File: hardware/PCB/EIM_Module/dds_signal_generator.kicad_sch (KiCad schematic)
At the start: 48 parts, among them J1 Conn_02x04, U1 AD9834BRUZ, U2 AD8130ARZ, Y2 75MHz

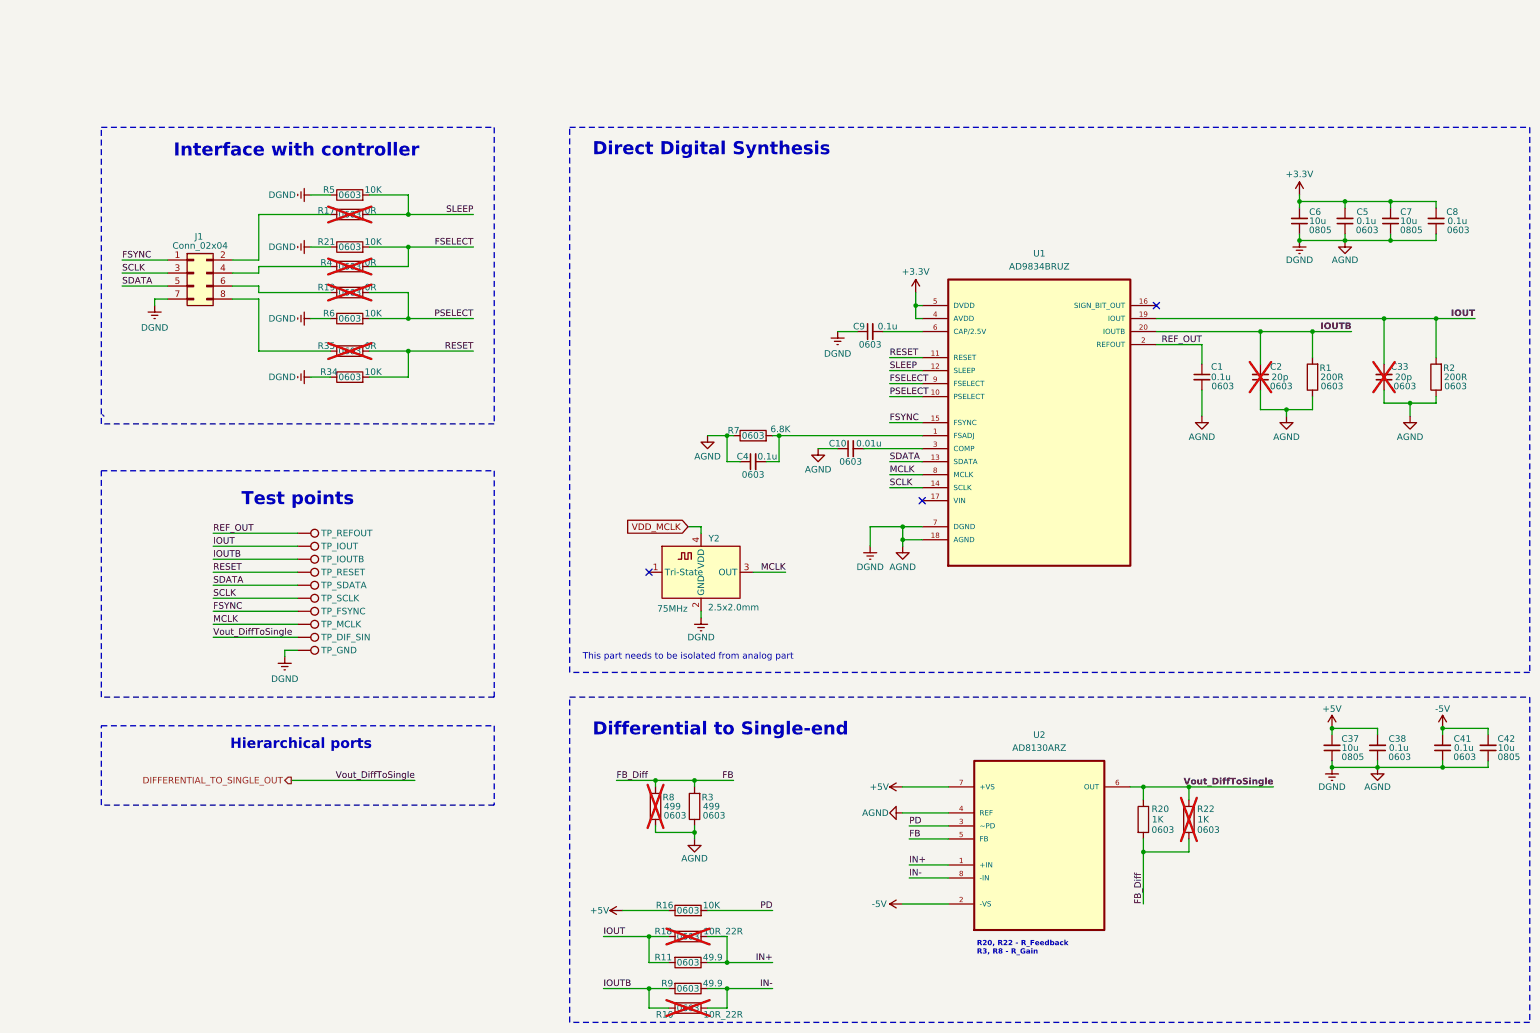
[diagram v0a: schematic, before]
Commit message: MAMS-33 Updated simulation final and update schematic and PCB
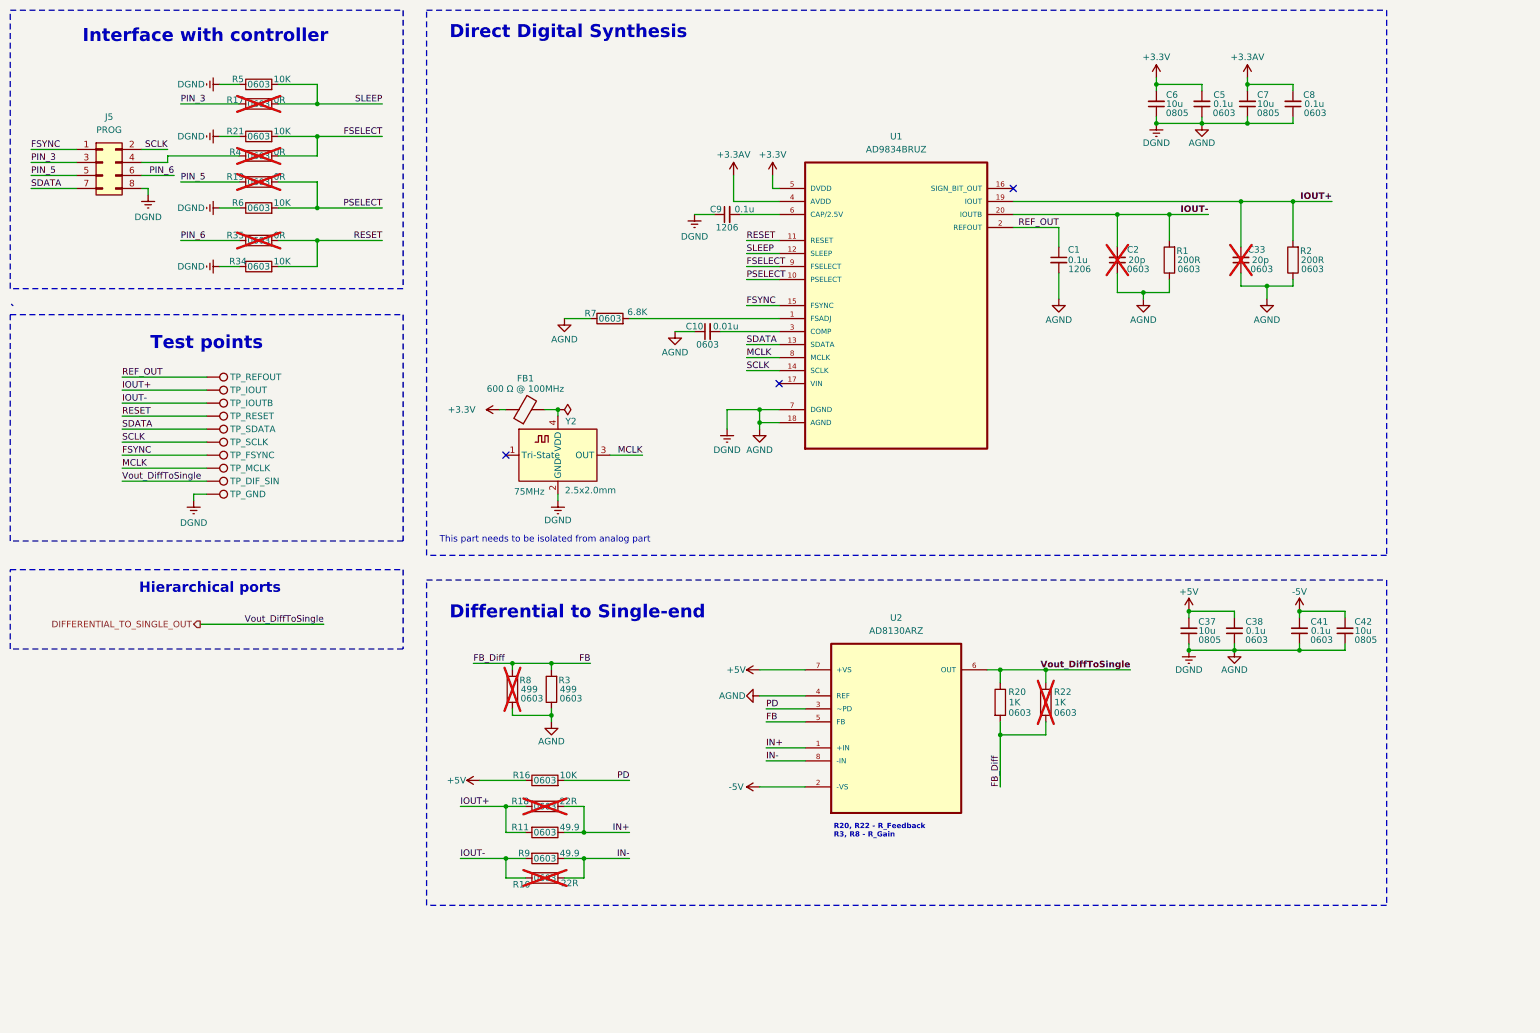
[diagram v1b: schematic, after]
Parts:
- removed C4: 0.1u, Capacitor_SMD:C_0603_1608Metric, symbol Device:C_Small
- removed J1: Conn_02x04, Connector_PinHeader_2.54mm:PinHeader_2x04_P2.54mm_Vertical, symbol Connector_Generic:Conn_02x04_Odd_Even
- added FB1: 600 Ω @ 100MHz, Inductor_SMD:L_0603_1608Metric, symbol Device:FerriteBead
- added J5: PROG, Connector_JST:JST_PH_S8B-PH-K_1x08_P2.00mm_Horizontal, symbol Connector_Generic:Conn_02x04_Odd_Even
- C1, C9: footprint Capacitor_SMD:C_0603_1608Metric -> Capacitor_SMD:C_1206_3216Metric; Size 0603 -> 1206
- R10, R18: value 10R_22R -> 22R
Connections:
- net +3.3V: now also FB1.1; no longer C7.2, C8.2, U1.4 (AVDD)
- net AGND: now also J5.8 (Pin_8)
- net FSYNC: now also J5.1 (Pin_1)
- net SCLK: now also J5.2 (Pin_2)
- net SDATA: now also J5.7 (Pin_7)
- net PIN_5: now reaches R19.1
- net PIN_5: now also J5.5 (Pin_5)
- net at R4.1: now also J5.4 (Pin_4)
- net PIN_3: now reaches R17.1
- net PIN_3: now also J5.3 (Pin_3)
- net PIN_6: now reaches R35.1
- net PIN_6: now also J5.6 (Pin_6)
- net IOUT renamed IOUT+
- net IOUTB renamed IOUT-
- net VDD_MCLK: no longer names the net of Y2.4 (VDD)
- net VDD_MCLK: now also FB1.2
- new net +3.3AV: C7.2, C8.2, U1.4 (AVDD)
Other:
- moved on the sheet: C1, C10, C2, C33, C37, C38, C41, C42, C5, C6, C7, C8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

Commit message: MAMS-38 updated PCB layout for EIM with version using connector
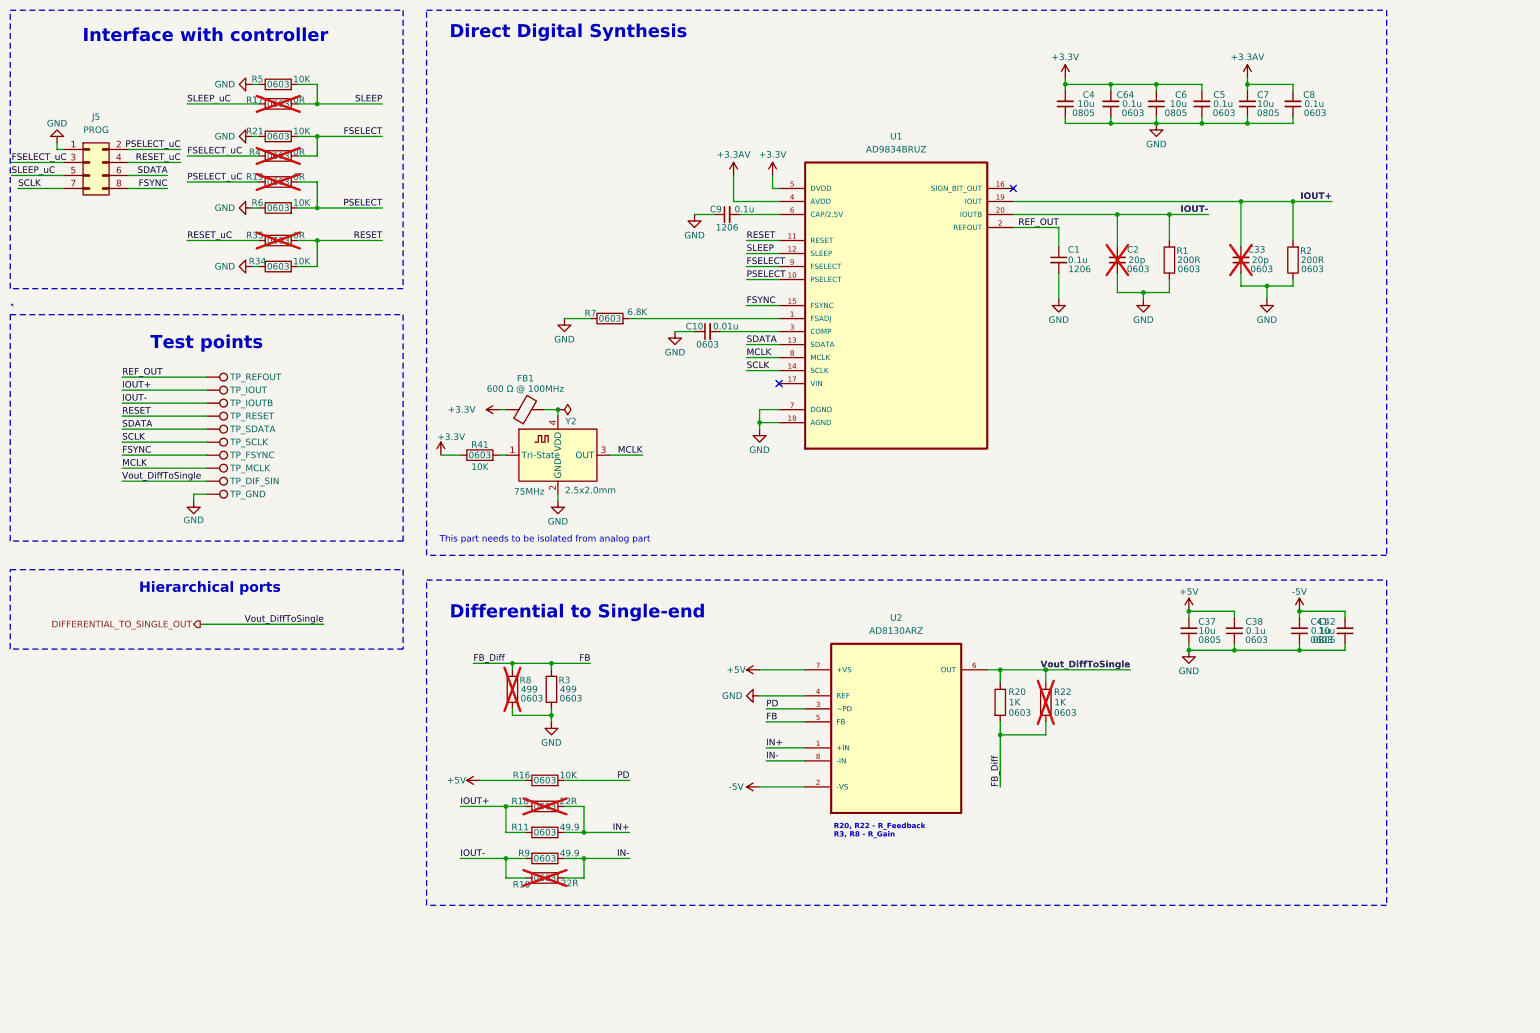
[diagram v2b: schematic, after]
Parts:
- added C4: 10u, Capacitor_SMD:C_0805_2012Metric, symbol Device:C_Small
- added C64: 0.1u, Capacitor_SMD:C_0603_1608Metric, symbol Device:C_Small
- added R41: 10K, Resistor_SMD:R_0603_1608Metric, symbol Device:R
- Y2: footprint Oscillator:Oscillator_SMD_ECS_2520MV-xxx-xx-4Pin_2.5x2.0mm -> Oscillator:Oscillator_SMD_SeikoEpson_SG210-4Pin_2.5x2.0mm
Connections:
- net +3.3V: now also C4.2, C64.2, R41.1
- net FSYNC: now also J5.8 (Pin_8); no longer J5.1 (Pin_1)
- net SCLK: now also J5.7 (Pin_7); no longer J5.2 (Pin_2)
- net SDATA: now also J5.6 (Pin_6); no longer J5.7 (Pin_7)
- net FSELECT_uC: now reaches R4.1
- net FSELECT_uC: now also J5.3 (Pin_3); no longer J5.4 (Pin_4)
- net at Y2.1 (Tri-State): now also R41.2
- net AGND renamed GND
- net GND: now also J5.1 (Pin_1), C4.1, C64.1; no longer J5.8 (Pin_8)
- net PIN_3 renamed SLEEP_uC
- net SLEEP_uC: now also J5.5 (Pin_5); no longer J5.3 (Pin_3)
- net PIN_5 renamed PSELECT_uC
- net PSELECT_uC: now also J5.2 (Pin_2); no longer J5.5 (Pin_5)
- net PIN_6 renamed RESET_uC
- net RESET_uC: now also J5.4 (Pin_4); no longer J5.6 (Pin_6)
- no-connect marks 3 -> 2
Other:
- moved on the sheet: C42, C6, J5, R17, R19, R21, R34, R35, R4, R5, R6

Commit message: MAMS-40 Updated PCB upto LPF
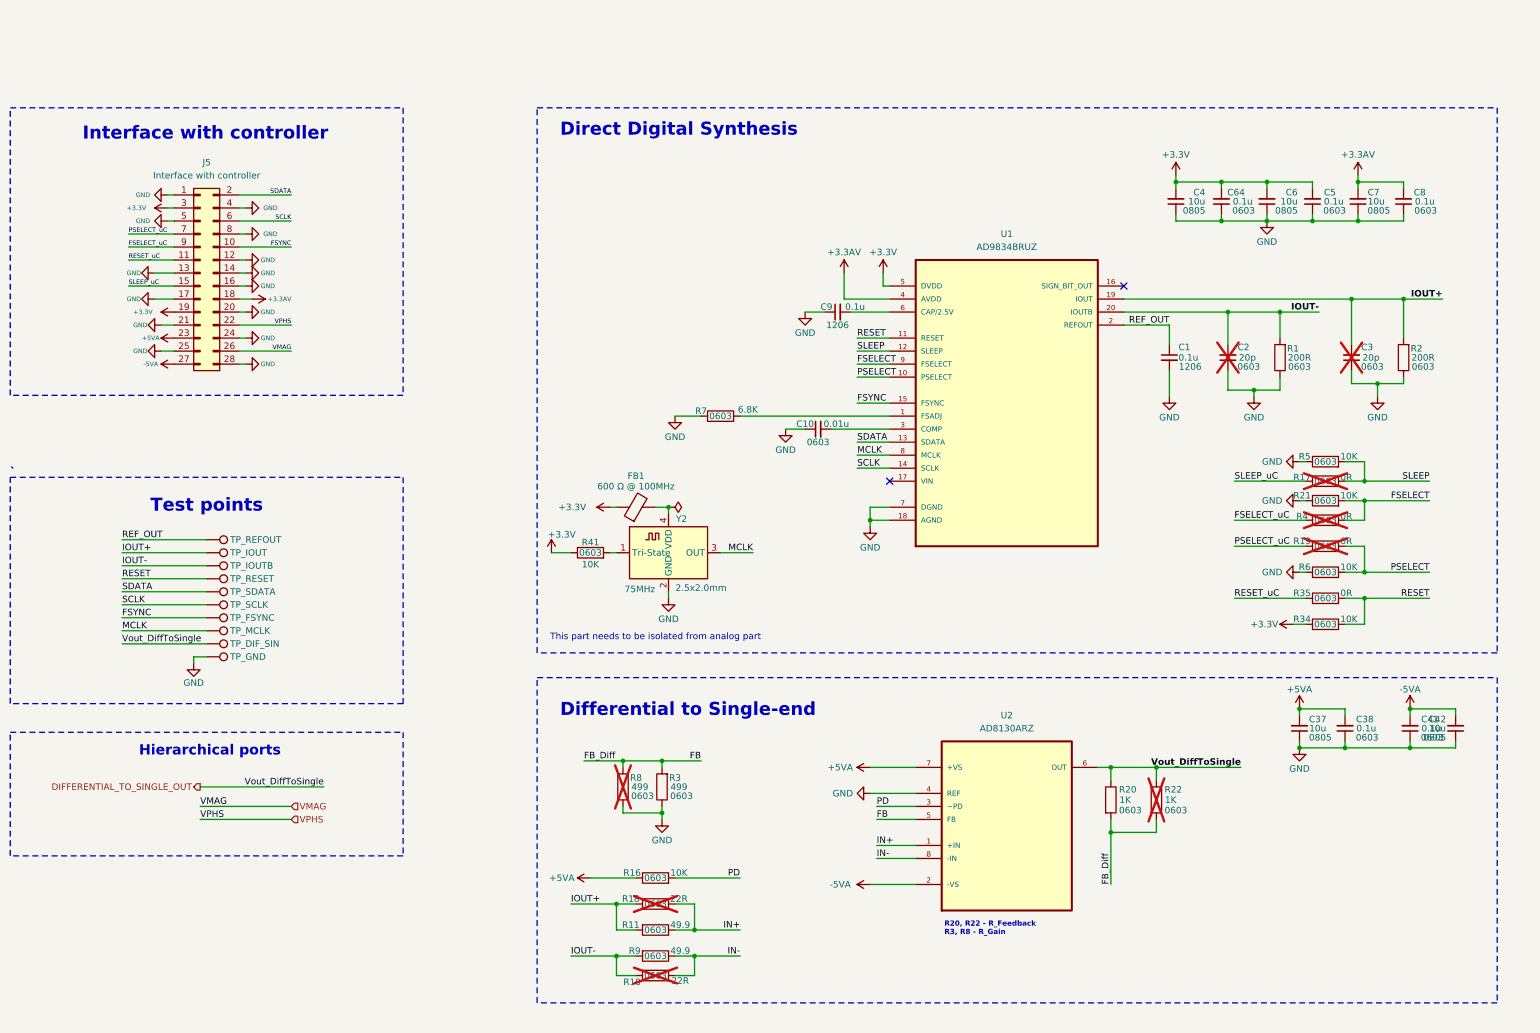
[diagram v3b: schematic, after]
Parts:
- removed J5: PROG, Connector_JST:JST_PH_S8B-PH-K_1x08_P2.00mm_Horizontal, symbol Connector_Generic:Conn_02x04_Odd_Even
- added J5: Interface with controller, Connector_PinHeader_2.00mm:PinHeader_2x14_P2.00mm_Vertical, symbol Connector_Generic:Conn_02x14_Odd_Even
- R35: now fitted
- renumbered C33 to C3
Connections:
- net +3.3AV: now also J5.18 (Pin_18)
- net +3.3V: now also R34.1, J5.19 (Pin_19), J5.3 (Pin_3)
- net FSELECT_uC: now also J5.9 (Pin_9)
- net FSYNC: now also J5.10 (Pin_10)
- net GND: now also J5.1 (Pin_1), J5.12 (Pin_12), J5.13 (Pin_13), J5.14 (Pin_14), J5.16 (Pin_16), J5.17 (Pin_17), J5.20 (Pin_20), J5.21 (Pin_21), J5.24 (Pin_24), J5.25 (Pin_25), J5.28 (Pin_28), J5.4 (Pin_4), J5.5 (Pin_5), J5.8 (Pin_8); no longer R34.1
- net PSELECT_uC: now also J5.7 (Pin_7)
- net RESET_uC: now also J5.11 (Pin_11)
- net SCLK: now also J5.6 (Pin_6)
- net SDATA: now also J5.2 (Pin_2)
- net SLEEP_uC: now also J5.15 (Pin_15)
- net +5V renamed +5VA
- net +5VA: now also J5.23 (Pin_23)
- net -5V renamed -5VA
- net -5VA: now also J5.27 (Pin_27)
- new net VMAG: J5.26 (Pin_26)
- new net VPHS: J5.22 (Pin_22)
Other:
- moved on the sheet: C1, C10, C2, C3, C37, C38, C4, C41, C42, C5, C6, C64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
